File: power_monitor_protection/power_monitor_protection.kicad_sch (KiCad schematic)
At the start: 0 parts

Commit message: feat: add power monitor protection circuitry
Signed-off-by: Scott Gibb <smgibb@yahoo.com>
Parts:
- added C1, C2: 10uF, symbol Device:C
- added C3, C4: 100nF, symbol Device:C
- added J1: Conn_01x05_Socket, symbol Connector:Conn_01x05_Socket
- added J2: Conn_01x04_Socket, symbol Connector:Conn_01x04_Socket
- added U1: ADuM1201AR, Package_SO:SOIC-8_3.9x4.9mm_P1.27mm, symbol Isolator:ADuM1201AR
- added U3: B0503S-1WR3, SIP4_B_S-1WR3_MNS, symbol 2026-06-24_20-18-09:B0505S-1WR3
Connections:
- new net 3V3_ISO: C2.1, C4.1, J2.1 (Pin_1), U1.8 (VDD2), U3.4 (+VO)
- new net 3V3_PI: C3.1, J1.2 (Pin_2), U1.1 (VDD1)
- new net 5V_PI: C1.1, J1.1 (Pin_1), U3.1 (GND)
- new net GND1: C1.2, C3.2, J1.5 (Pin_5), U1.4 (GND1), U3.2 (VIN)
- new net GND2: C2.2, C4.2, J2.4 (Pin_4), U1.5 (GND2), U3.3 (0V)
- new net PI_ISO_RX: J2.3 (Pin_3), U1.6 (VOB)
- new net PI_ISO_TX: J2.2 (Pin_2), U1.7 (VIA)
- new net PI_RX: J1.4 (Pin_4), U1.3 (VIB)
- new net PI_TX: J1.3 (Pin_3), U1.2 (VOA)

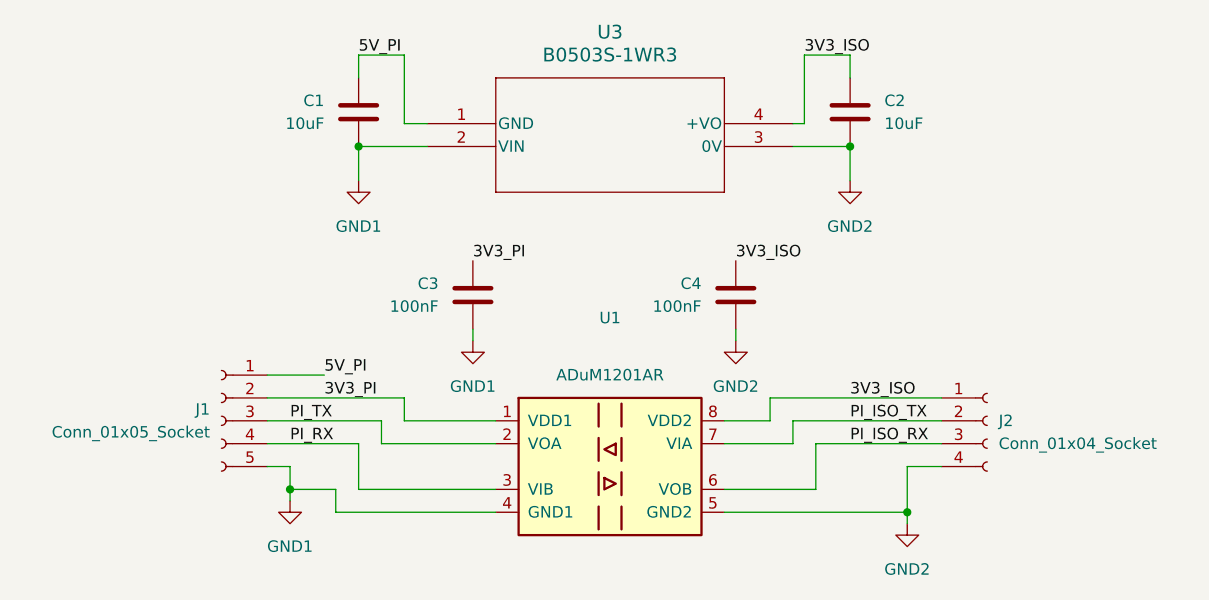
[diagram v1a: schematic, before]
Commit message: feat: add extra caps to power protection circuit
Signed-off-by: Scott Gibb <smgibb@yahoo.com>
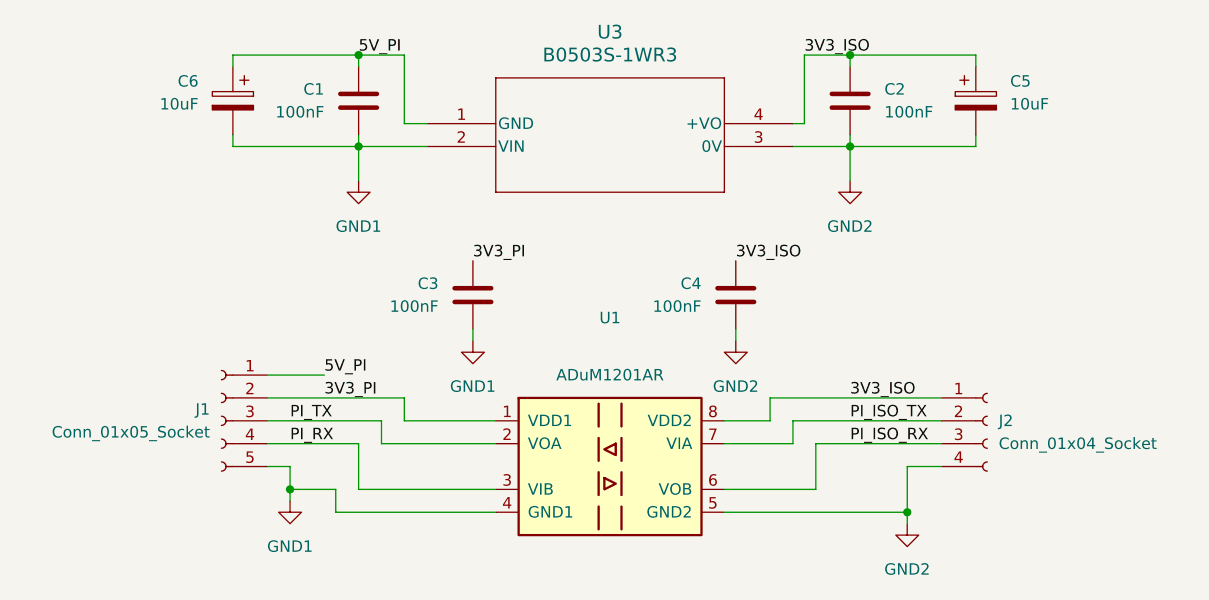
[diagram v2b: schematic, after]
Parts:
- added C5, C6: 10uF, symbol Device:C_Polarized
- C1, C2: value 10uF -> 100nF
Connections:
- net 3V3_ISO: now also C5.1
- net 5V_PI: now also C6.1
- net GND1: now also C6.2
- net GND2: now also C5.2
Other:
- moved on the sheet: C1, C2
